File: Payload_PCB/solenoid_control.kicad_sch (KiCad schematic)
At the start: 5 parts, among them Q2 NMOS

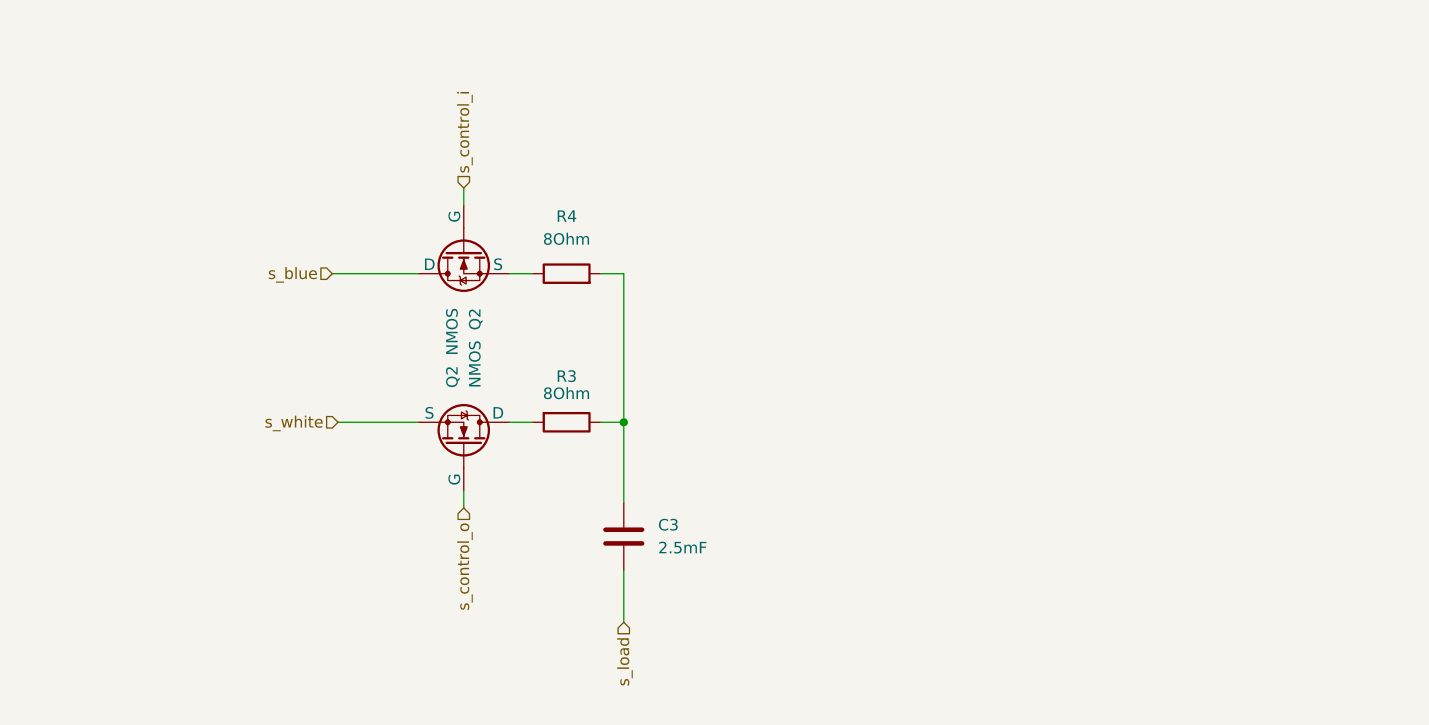
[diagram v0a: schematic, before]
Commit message: Added Symbols and Footprints
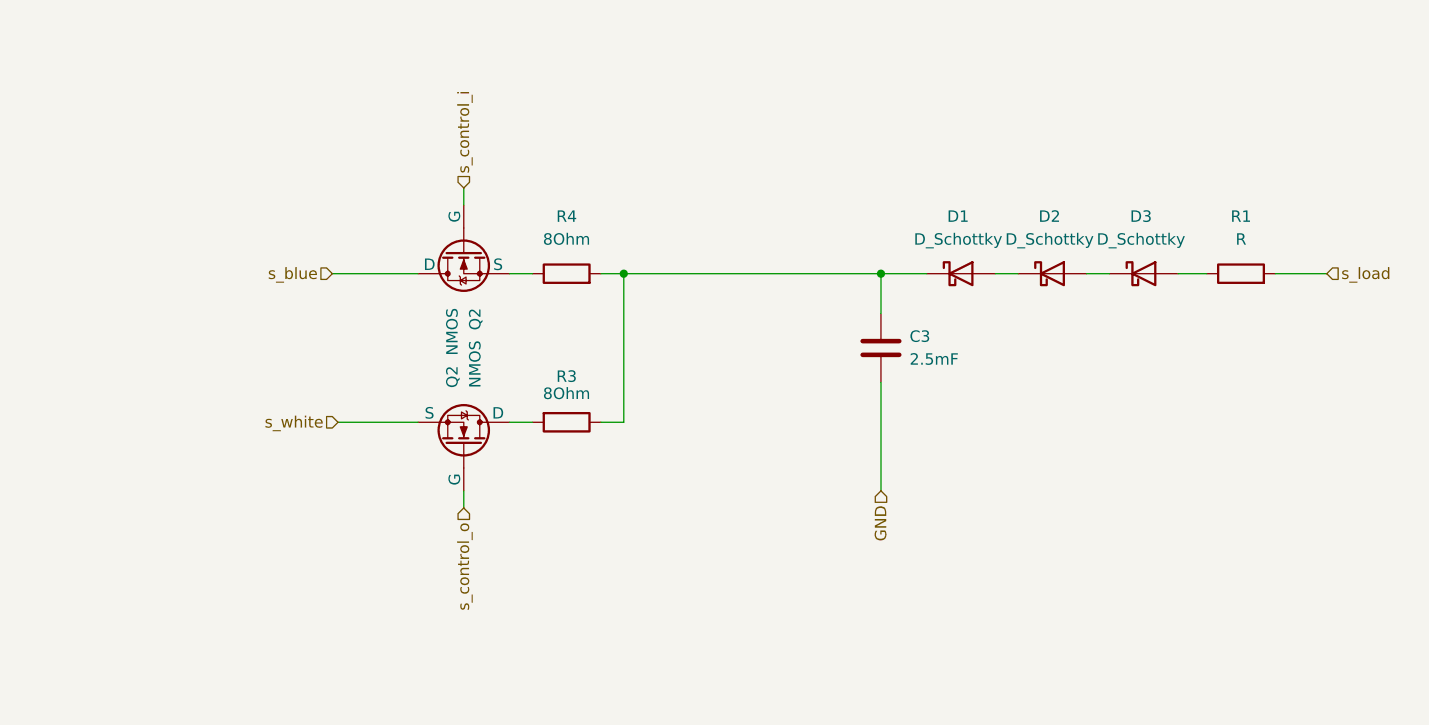
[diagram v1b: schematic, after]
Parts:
- added D1, D2, D3: D_Schottky, symbol Device:D_Schottky
- added R1: R, symbol Device:R
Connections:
- net s_load: now also R1.2; no longer C3.2
- net at R3.1, R4.2: now also C3.2, D1.1 (K); no longer C3.1
- new net: D2.2 (A), D3.1 (K)
- new net: D3.2 (A), R1.1
- new net: D1.2 (A), D2.1 (K)
- new net GND: C3.1
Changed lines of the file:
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@@
 (kicad_sch (version 20230121) (generator eeschema)
   (paper "A4")
-  (junction (at 107.95 71.12) (diameter 0) (color 0 0 0 0)
+  (junction (at 136.525 54.61) (diameter 0) (color 0 0 0 0)
+  )
+  (junction (at 107.95 54.61) (diameter 0) (color 0 0 0 0)
+  )
+  (wire (pts (xy 169.545 54.61) (xy 172.72 54.61))
+    (stroke (width 0) (type default))
+  )
+  (wire (pts (xy 107.95 54.61) (xy 136.525 54.61))
+    (stroke (width 0) (type default))
   )
   (wire (pts (xy 95.25 54.61) (xy 97.79 54.61))
@@
     (stroke (width 0) (type default))
   )
-  (wire (pts (xy 107.95 87.63) (xy 107.95 93.345))
+  (wire (pts (xy 136.525 54.61) (xy 136.525 59.055))
     (stroke (width 0) (type default))
   )
@@
     (stroke (width 0) (type default))
   )
-  (wire (pts (xy 107.95 71.12) (xy 107.95 80.01))
+  (wire (pts (xy 136.525 66.675) (xy 136.525 78.74))
+    (stroke (width 0) (type default))
+  )
+  (wire (pts (xy 186.055 54.61) (xy 180.34 54.61))
     (stroke (width 0) (type default))
   )
@@
     (stroke (width 0) (type default))
   )
+  (wire (pts (xy 161.925 54.61) (xy 159.385 54.61))
+    (stroke (width 0) (type default))
+  )
+  (wire (pts (xy 136.525 54.61) (xy 141.605 54.61))
+    (stroke (width 0) (type default))
+  )
   (wire (pts (xy 107.95 54.61) (xy 107.95 71.12))
+    (stroke (width 0) (type default))
+  )
+  (wire (pts (xy 151.765 54.61) (xy 149.225 54.61))
     (stroke (width 0) (type default))
   )
@@
     (effects (font (size 1.27 1.27)) (justify left))
   )
-  (hierarchical_label "s_load" (shape input) (at 107.95 93.345 270) (fields_autoplaced)
-    (effects (font (size 1.27 1.27)) (justify right))
-  )
   (hierarchical_label "s_blue" (shape input) (at 75.565 54.61 180) (fields_autoplaced)
     (effects (font (size 1.27 1.27)) (justify right))
@@
     (effects (font (size 1.27 1.27)) (justify right))
   )
+  (hierarchical_label "GND" (shape input) (at 136.525 78.74 270) (fields_autoplaced)
+    (effects (font (size 1.27 1.27)) (justify right))
+  )
+  (hierarchical_label "s_load" (shape input) (at 186.055 54.61 0) (fields_autoplaced)
+    (effects (font (size 1.27 1.27)) (justify left))
+  )
   (hierarchical_label "s_white" (shape input) (at 76.2 71.12 180) (fields_autoplaced)
     (effects (font (size 1.27 1.27)) (justify right))
+  )
+  (symbol (lib_id "Device:D_Schottky") (at 165.735 54.61 0) (unit 1)
+    (in_bom yes) (on_board yes) (dnp no) (fields_autoplaced)
+    (property "Reference" "D3" (at 165.4175 48.26 0)
+      (effects (font (size 1.27 1.27)))
+    )
+    (property "Value" "D_Schottky" (at 165.4175 50.8 0)
+      (effects (font (size 1.27 1.27)))
+    )
+    (property "Footprint" "" (at 165.735 54.61 0)
+      (effects (font (size 1.27 1.27)) hide)
+    )
+    (property "Datasheet" "~" (at 165.735 54.61 0)
+      (effects (font (size 1.27 1.27)) hide)
+    )
+    (pin "1")
+    (pin "2")
+    (instances
+      (project "Payload_PCB"
+        (path "/5c4f9a68-5778-4223-b18a-2e31db8d7d40/d35d8bfb-c080-4ec9-8d57-2a69a0b715d8"
+          (reference "D3") (unit 1)
+        )
+        (path "/5c4f9a68-5778-4223-b18a-2e31db8d7d40/7b4c1a27-0edc-40a8-bad5-7c7578297bdc"
+          (reference "D3") (unit 1)
+        )
+        (path "/5c4f9a68-5778-4223-b18a-2e31db8d7d40/83f3690e-358b-48b8-8f73-86eaa2f08e98"
+          (reference "D3") (unit 1)
+        )
+      )
+      (project "solenoid_control"
+        (path "/d35e6abe-7670-4b21-9efa-e973c38a6f4f"
+          (reference "D3") (unit 1)
+        )
+      )
+    )
   )
   (symbol (lib_id "Simulation_SPICE:NMOS") (at 90.17 52.07 90) (mirror x) (unit 1)
@@
     )
   )
-  (symbol (lib_id "Device:C") (at 107.95 83.82 0) (unit 1)
-    (in_bom yes) (on_board yes) (dnp no) (fields_autoplaced)
-    (property "Reference" "C3" (at 111.76 82.55 0)
-      (effects (font (size 1.27 1.27)) (justify left))
-    )
-    (property "Value" "2.5mF" (at 111.76 85.09 0)
-      (effects (font (size 1.27 1.27)) (justify left))
-    )
-    (property "Footprint" "" (at 108.9152 87.63 0)
-      (effects (font (size 1.27 1.27)) hide)
-    )
-    (property "Datasheet" "~" (at 107.95 83.82 0)
+  (symbol (lib_id "Device:D_Schottky") (at 145.415 54.61 0) (unit 1)
+    (in_bom yes) (on_board yes) (dnp no) (fields_autoplaced)
+    (property "Reference" "D1" (at 145.0975 48.26 0)
+      (effects (font (size 1.27 1.27)))
+    )
+    (property "Value" "D_Schottky" (at 145.0975 50.8 0)
+      (effects (font (size 1.27 1.27)))
+    )
+    (property "Footprint" "" (at 145.415 54.61 0)
+      (effects (font (size 1.27 1.27)) hide)
+    )
+    (property "Datasheet" "~" (at 145.415 54.61 0)
+      (effects (font (size 1.27 1.27)) hide)
+    )
+    (pin "1")
+    (pin "2")
+    (instances
+      (project "Payload_PCB"
+        (path "/5c4f9a68-5778-4223-b18a-2e31db8d7d40/d35d8bfb-c080-4ec9-8d57-2a69a0b715d8"
+          (reference "D1") (unit 1)
+        )
+        (path "/5c4f9a68-5778-4223-b18a-2e31db8d7d40/7b4c1a27-0edc-40a8-bad5-7c7578297bdc"
+          (reference "D1") (unit 1)
+        )
+        (path "/5c4f9a68-5778-4223-b18a-2e31db8d7d40/83f3690e-358b-48b8-8f73-86eaa2f08e98"
+          (reference "D1") (unit 1)
+        )
+      )
+      (project "solenoid_control"
+        (path "/d35e6abe-7670-4b21-9efa-e973c38a6f4f"
+          (reference "D1") (unit 1)
+        )
+      )
+    )
+  )
+  (symbol (lib_id "Device:D_Schottky") (at 155.575 54.61 0) (unit 1)
+    (in_bom yes) (on_board yes) (dnp no) (fields_autoplaced)
+    (property "Reference" "D2" (at 155.2575 48.26 0)
+      (effects (font (size 1.27 1.27)))
+    )
+    (property "Value" "D_Schottky" (at 155.2575 50.8 0)
+      (effects (font (size 1.27 1.27)))
+    )
+    (property "Footprint" "" (at 155.575 54.61 0)
+      (effects (font (size 1.27 1.27)) hide)
+    )
+    (property "Datasheet" "~" (at 155.575 54.61 0)
+      (effects (font (size 1.27 1.27)) hide)
+    )
+    (pin "1")
+    (pin "2")
+    (instances
+      (project "Payload_PCB"
+        (path "/5c4f9a68-5778-4223-b18a-2e31db8d7d40/d35d8bfb-c080-4ec9-8d57-2a69a0b715d8"
+          (reference "D2") (unit 1)
+        )
+        (path "/5c4f9a68-5778-4223-b18a-2e31db8d7d40/7b4c1a27-0edc-40a8-bad5-7c7578297bdc"
+          (reference "D2") (unit 1)
+        )
+        (path "/5c4f9a68-5778-4223-b18a-2e31db8d7d40/83f3690e-358b-48b8-8f73-86eaa2f08e98"
+          (reference "D2") (unit 1)
+        )
+      )
+      (project "solenoid_control"
+        (path "/d35e6abe-7670-4b21-9efa-e973c38a6f4f"
+          (reference "D2") (unit 1)
+        )
+      )
+    )
+  )
+  (symbol (lib_id "Device:R") (at 176.53 54.61 90) (unit 1)
+    (in_bom yes) (on_board yes) (dnp no) (fields_autoplaced)
+    (property "Reference" "R1" (at 176.53 48.26 90)
+      (effects (font (size 1.27 1.27)))
+    )
+    (property "Value" "R" (at 176.53 50.8 90)
+      (effects (font (size 1.27 1.27)))
+    )
+    (property "Footprint" "" (at 176.53 56.388 90)
+      (effects (font (size 1.27 1.27)) hide)
+    )
+    (property "Datasheet" "~" (at 176.53 54.61 0)
+      (effects (font (size 1.27 1.27)) hide)
+    )
+    (pin "1")
+    (pin "2")
+    (instances
+      (project "Payload_PCB"
+        (path "/5c4f9a68-5778-4223-b18a-2e31db8d7d40/d35d8bfb-c080-4ec9-8d57-2a69a0b715d8"
+          (reference "R1") (unit 1)
+        )
+        (path "/5c4f9a68-5778-4223-b18a-2e31db8d7d40/7b4c1a27-0edc-40a8-bad5-7c7578297bdc"
+          (reference "R1") (unit 1)
+        )
+        (path "/5c4f9a68-5778-4223-b18a-2e31db8d7d40/83f3690e-358b-48b8-8f73-86eaa2f08e98"
+          (reference "R1") (unit 1)
+        )
+      )
+      (project "solenoid_control"
+        (path "/d35e6abe-7670-4b21-9efa-e973c38a6f4f"
+          (reference "R1") (unit 1)
+        )
+      )
+    )
+  )
+  (symbol (lib_id "Device:C") (at 136.525 62.865 180) (unit 1)
+    (in_bom yes) (on_board yes) (dnp no) (fields_autoplaced)
+    (property "Reference" "C3" (at 139.7 61.595 0)
+      (effects (font (size 1.27 1.27)) (justify right))
+    )
+    (property "Value" "2.5mF" (at 139.7 64.135 0)
+      (effects (font (size 1.27 1.27)) (justify right))
+    )
+    (property "Footprint" "" (at 135.5598 59.055 0)
+      (effects (font (size 1.27 1.27)) hide)
+    )
+    (property "Datasheet" "~" (at 136.525 62.865 0)
       (effects (font (size 1.27 1.27)) hide)
     )
@@
       (project "solenoid_control"
         (path "/d35e6abe-7670-4b21-9efa-e973c38a6f4f"
-          (reference "C3") (unit 1)
-        )
-      )
+          (reference "C1") (unit 1)
+        )
+      )

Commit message: Minor changes and corrections
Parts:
- removed D2, D3: D_Schottky, symbol Device:D_Schottky
- R7: renamed from R1; value R -> 10kOhm
- renumbered D1 to D6, R4 to R5, R3 to R6
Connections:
- net at R7.1: now also D6.2 (A)
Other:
- moved on the sheet: R7

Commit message: Changed some radio silence
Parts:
- added Q29: NMOS, symbol Simulation_SPICE:NMOS
- added R77: 5kOhm, symbol Device:R
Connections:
- net GND: now also Q29.3 (S)
- net at C3.2, D6.1 (K), R5.2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: now also R77.1
- new net: Q29.1 (D), R77.2
- new net Short/Discharge: Q29.2 (G)
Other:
- moved on the sheet: C3
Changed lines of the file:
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@@
 (kicad_sch (version 20230121) (generator eeschema)
   (paper "A4")
-  (junction (at 136.525 54.61) (diameter 0) (color 0 0 0 0)
+  (junction (at 139.7 54.61) (diameter 0) (color 0 0 0 0)
+  )
+  (junction (at 139.7 63.5) (diameter 0) (color 0 0 0 0)
+  )
+  (junction (at 139.7 80.645) (diameter 0) (color 0 0 0 0)
   )
   (junction (at 107.95 54.61) (diameter 0) (color 0 0 0 0)
@@
     (stroke (width 0) (type default))
   )
-  (wire (pts (xy 107.95 54.61) (xy 136.525 54.61))
+  (wire (pts (xy 128.905 63.5) (xy 126.365 63.5))
     (stroke (width 0) (type default))
   )
@@
     (stroke (width 0) (type default))
   )
+  (wire (pts (xy 139.7 80.645) (xy 139.7 87.63))
+    (stroke (width 0) (type default))
+  )
   (wire (pts (xy 76.2 71.12) (xy 85.09 71.12))
     (stroke (width 0) (type default))
   )
-  (wire (pts (xy 136.525 54.61) (xy 136.525 59.055))
+  (wire (pts (xy 139.7 54.61) (xy 139.7 63.5))
     (stroke (width 0) (type default))
   )
@@
     (stroke (width 0) (type default))
   )
-  (wire (pts (xy 136.525 66.675) (xy 136.525 78.74))
+  (wire (pts (xy 139.7 75.565) (xy 139.7 80.645))
+    (stroke (width 0) (type default))
+  )
+  (wire (pts (xy 118.745 78.74) (xy 118.745 72.39))
+    (stroke (width 0) (type default))
+  )
+  (wire (pts (xy 139.7 54.61) (xy 141.605 54.61))
     (stroke (width 0) (type default))
   )
@@
     (stroke (width 0) (type default))
   )
+  (wire (pts (xy 126.365 77.47) (xy 126.365 80.645))
+    (stroke (width 0) (type default))
+  )
+  (wire (pts (xy 136.525 63.5) (xy 139.7 63.5))
+    (stroke (width 0) (type default))
+  )
   (wire (pts (xy 75.565 54.61) (xy 85.09 54.61))
     (stroke (width 0) (type default))
   )
+  (wire (pts (xy 126.365 80.645) (xy 139.7 80.645))
+    (stroke (width 0) (type default))
+  )
   (wire (pts (xy 90.17 78.74) (xy 90.17 80.645))
     (stroke (width 0) (type default))
   )
+  (wire (pts (xy 139.7 63.5) (xy 139.7 67.945))
+    (stroke (width 0) (type default))
+  )
   (wire (pts (xy 105.41 71.12) (xy 107.95 71.12))
     (stroke (width 0) (type default))
   )
-  (wire (pts (xy 136.525 54.61) (xy 141.605 54.61))
-    (stroke (width 0) (type default))
-  )
   (wire (pts (xy 107.95 54.61) (xy 107.95 71.12))
     (stroke (width 0) (type default))
   )
+  (wire (pts (xy 107.95 54.61) (xy 139.7 54.61))
+    (stroke (width 0) (type default))
+  )
   (wire (pts (xy 156.845 54.61) (xy 149.225 54.61))
     (stroke (width 0) (type default))
   )
+  (wire (pts (xy 126.365 63.5) (xy 126.365 67.31))
+    (stroke (width 0) (type default))
+  )
   (wire (pts (xy 105.41 54.61) (xy 107.95 54.61))
     (stroke (width 0) (type default))
+  )
+  (global_label "Short{slash}Discharge" (shape input) (at 118.745 78.74 180) (fields_autoplaced)
+    (effects (font (size 1.27 1.27)) (justify right))
+    (property "Intersheetrefs" "${INTERSHEET_REFS}" (at 100.0966 78.74 0)
+      (effects (font (size 1.27 1.27)) (justify right) hide)
+    )
   )
   (hierarchical_label "s_control_i" (shape input) (at 90.17 45.085 90) (fields_autoplaced)
@@
     (effects (font (size 1.27 1.27)) (justify right))
   )
-  (hierarchical_label "GND" (shape input) (at 136.525 78.74 270) (fields_autoplaced)
+  (hierarchical_label "GND" (shape input) (at 139.7 87.63 270) (fields_autoplaced)
     (effects (font (size 1.27 1.27)) (justify right))
   )
@@
   (hierarchical_label "s_white" (shape input) (at 76.2 71.12 180) (fields_autoplaced)
     (effects (font (size 1.27 1.27)) (justify right))
+  )
+  (symbol (lib_id "Simulation_SPICE:NMOS") (at 123.825 72.39 0) (unit 1)
+    (in_bom yes) (on_board yes) (dnp no) (fields_autoplaced)
+    (property "Reference" "Q29" (at 129.54 71.12 0)
+      (effects (font (size 1.27 1.27)) (justify left))
+    )
+    (property "Value" "NMOS" (at 129.54 73.66 0)
+      (effects (font (size 1.27 1.27)) (justify left))
+    )
+    (property "Footprint" "" (at 128.905 69.85 0)
+      (effects (font (size 1.27 1.27)) hide)
+    )
+    (property "Datasheet" "https://ngspice.sourceforge.io/docs/ngspice-manual.pdf" (at 123.825 85.09 0)
+      (effects (font (size 1.27 1.27)) hide)
+    )
+    (property "Sim.Device" "NMOS" (at 123.825 89.535 0)
+      (effects (font (size 1.27 1.27)) hide)
+    )
+    (property "Sim.Type" "VDMOS" (at 123.825 91.44 0)
+      (effects (font (size 1.27 1.27)) hide)
+    )
+    (property "Sim.Pins" "1=D 2=G 3=S" (at 123.825 87.63 0)
+      (effects (font (size 1.27 1.27)) hide)
+    )
+    (pin "1")
+    (pin "2")
+    (pin "3")
+    (instances
+      (project "Payload_PCB"
+        (path "/5c4f9a68-5778-4223-b18a-2e31db8d7d40/ae559297-2f69-4b2e-9656-464d0c3b2422"
+          (reference "Q29") (unit 1)
+        )
+        (path "/5c4f9a68-5778-4223-b18a-2e31db8d7d40/d35d8bfb-c080-4ec9-8d57-2a69a0b715d8"
+          (reference "Q26") (unit 1)
+        )
+        (path "/5c4f9a68-5778-4223-b18a-2e31db8d7d40/7b4c1a27-0edc-40a8-bad5-7c7578297bdc"
+          (reference "Q27") (unit 1)
+        )
+        (path "/5c4f9a68-5778-4223-b18a-2e31db8d7d40/83f3690e-358b-48b8-8f73-86eaa2f08e98"
+          (reference "Q28") (unit 1)
+        )
+      )
+    )
   )
   (symbol (lib_id "Simulation_SPICE:NMOS") (at 90.17 52.07 90) (mirror x) (unit 1)
@@
     )
   )
-  (symbol (lib_id "Device:C") (at 136.525 62.865 180) (unit 1)
+  (symbol (lib_id "Device:R") (at 132.715 63.5 270) (unit 1)
+    (in_bom yes) (on_board yes) (dnp no)
+    (property "Reference" "R77" (at 132.715 59.055 90)
+      (effects (font (size 1.27 1.27)))
+    )
+    (property "Value" "5kOhm" (at 132.715 60.96 90)
+      (effects (font (size 1.27 1.27)))
+    )
+    (property "Footprint" "" (at 132.715 61.722 90)
+      (effects (font (size 1.27 1.27)) hide)
+    )
+    (property "Datasheet" "~" (at 132.715 63.5 0)
+      (effects (font (size 1.27 1.27)) hide)
+    )
+    (pin "1")
+    (pin "2")
+    (instances
+      (project "Payload_PCB"
+        (path "/5c4f9a68-5778-4223-b18a-2e31db8d7d40/ae559297-2f69-4b2e-9656-464d0c3b2422"
+          (reference "R77") (unit 1)
+        )
+        (path "/5c4f9a68-5778-4223-b18a-2e31db8d7d40/d35d8bfb-c080-4ec9-8d57-2a69a0b715d8"
+          (reference "R74") (unit 1)
+        )
+        (path "/5c4f9a68-5778-4223-b18a-2e31db8d7d40/7b4c1a27-0edc-40a8-bad5-7c7578297bdc"
+          (reference "R75") (unit 1)
+        )
+        (path "/5c4f9a68-5778-4223-b18a-2e31db8d7d40/83f3690e-358b-48b8-8f73-86eaa2f08e98"
+          (reference "R76") (unit 1)
+        )
+      )
+    )
+  )
+  (symbol (lib_id "Device:C") (at 139.7 71.755 180) (unit 1)
     (in_bom yes) (on_board yes) (dnp no) (fields_autoplaced)
-    (property "Reference" "C3" (at 139.7 61.595 0)
+    (property "Reference" "C3" (at 142.875 70.485 0)
       (effects (font (size 1.27 1.27)) (justify right))
     )
-    (property "Value" "2.5mF" (at 139.7 64.135 0)
+    (property "Value" "2.5mF" (at 142.875 73.025 0)
       (effects (font (size 1.27 1.27)) (justify right))
     )
-    (property "Footprint" "" (at 135.5598 59.055 0)
-      (effects (font (size 1.27 1.27)) hide)
-    )
-    (property "Datasheet" "~" (at 136.525 62.865 0)
-      (effects (font (size 1.27 1.27)) hide)
-    )
+    (property "Footprint" "" (at 138.7348 67.945 0)
+      (effects (font (size 1.27 1.27)) hide)
+    )
+    (property "Datasheet" "~" (at 139.7 71.755 0)
+      (effects (font (size 1.27 1.27)) hide)
+    )
